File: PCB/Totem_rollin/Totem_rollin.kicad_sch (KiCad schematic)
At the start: 90 parts, among them U1 xiao-ble, U2 xiao-ble

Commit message: update
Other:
- note added: "R O L L E R E N C O D E R"
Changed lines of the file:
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@@
+		)
+	)
+	(text "R O L L E R\nE N C O D E R"
+		(exclude_from_sim no)
+		(at 110.998 57.912 0)
+		(effects
+			(font
+				(size 1.5 1.5)
+				(thickness 0.3)
+				(bold yes)
+			)
+			(justify left bottom)
 		)
 	)
@@
 		(effects
 			(font
+				(size 1.5 1.5)
+				(thickness 0.3)
+				(bold yes)
+			)
+			(justify left bottom)
+		)
+	)
+	(text "R O L L E R\nE N C O D E R"
+		(exclude_from_sim no)
+		(at 164.084 58.42 0)
+		(effects
+			(font

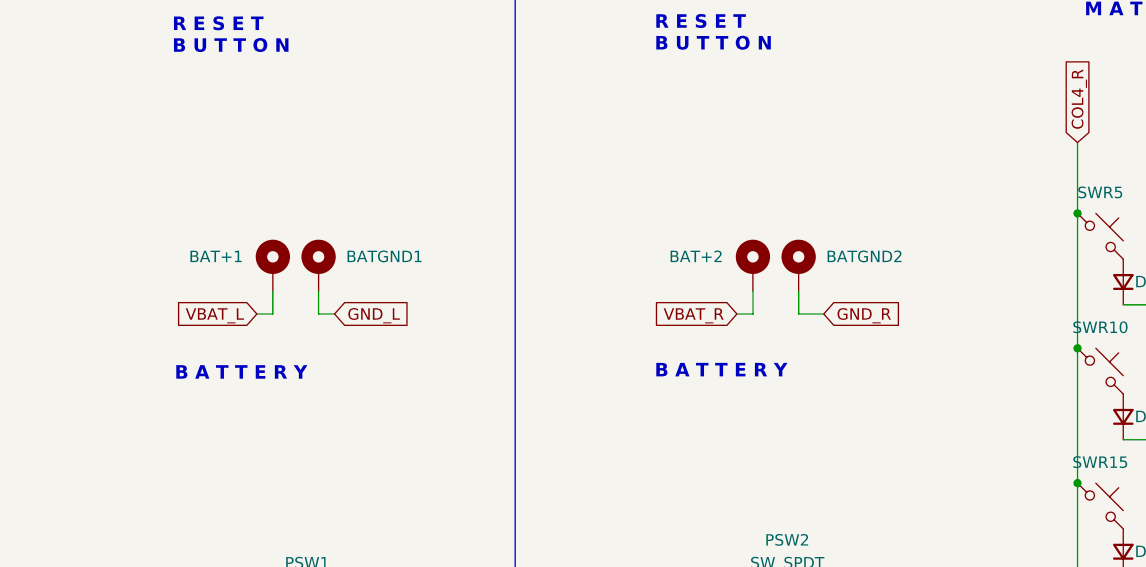
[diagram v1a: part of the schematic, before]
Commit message: add jst connector for battery
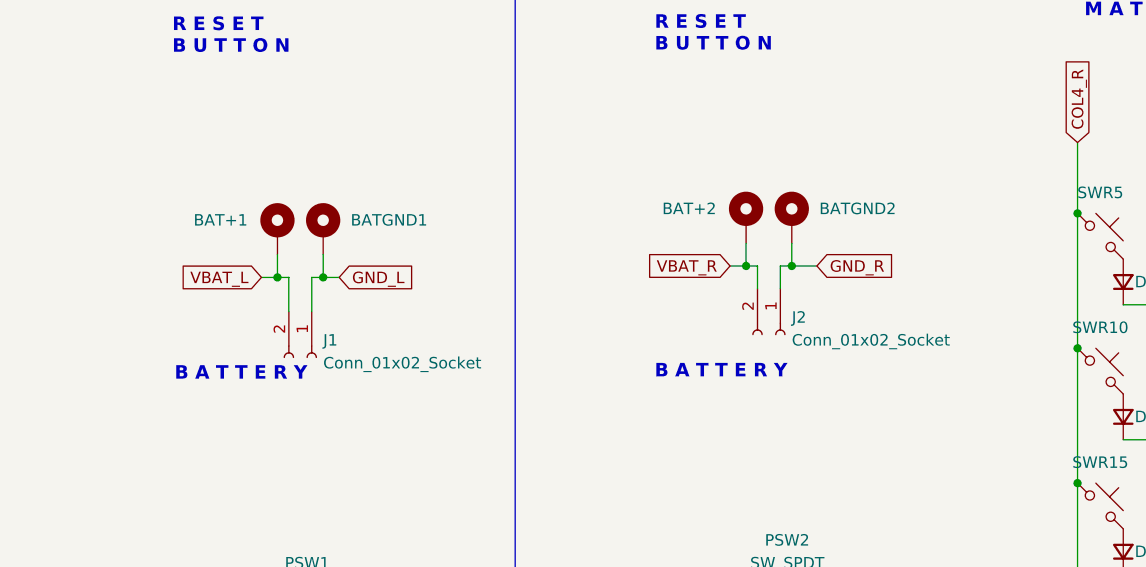
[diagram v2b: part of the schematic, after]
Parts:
- added J1, J2: Conn_01x02_Socket, symbol Connector:Conn_01x02_Socket
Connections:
- net GND_L: now also J1.1 (Pin_1)
- net GND_R: now also J2.1 (Pin_1)
- net VBAT_L: now also J1.2 (Pin_2)
- net VBAT_R: now also J2.2 (Pin_2)
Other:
- moved on the sheet: BAT+1, BAT+2, BATGND1, BATGND2
